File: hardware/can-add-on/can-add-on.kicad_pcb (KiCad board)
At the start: 2 copper layers, 48 x 40 mm, 38 parts

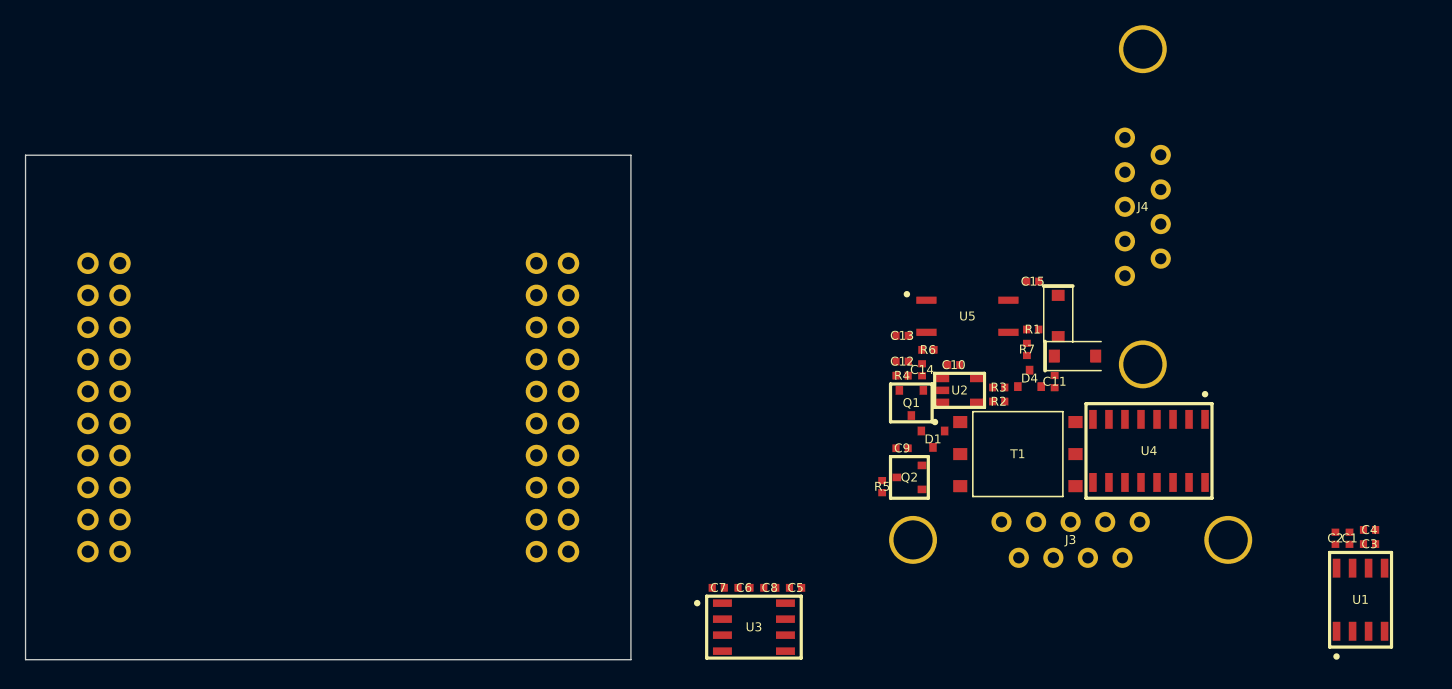
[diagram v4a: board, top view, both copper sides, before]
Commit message: Regenerate kicad with power/gnd symbols
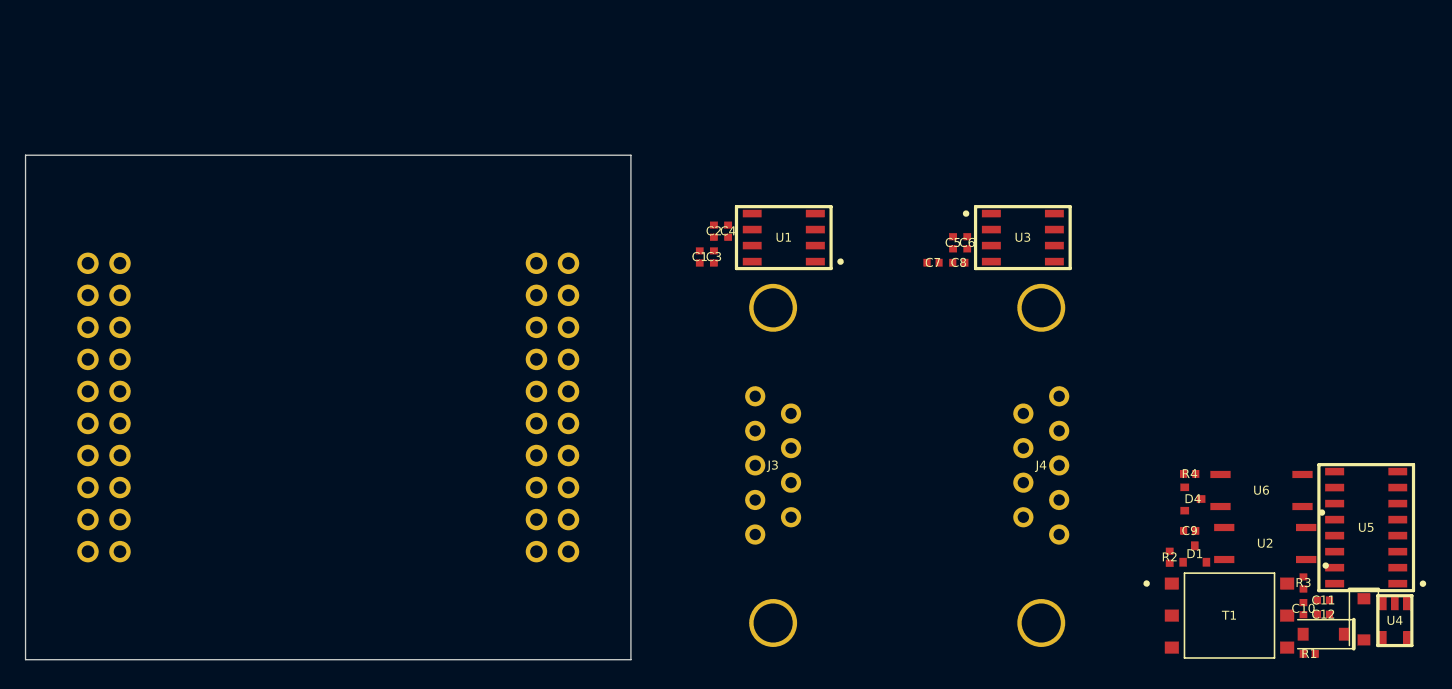
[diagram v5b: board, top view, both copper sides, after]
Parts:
- removed the ? at (206.4, 97.7)
- removed the ? at (207.7, 100.9)
- removed C13, C14, C15, R5, R6, R7: , can-add-on:ipc-two-pin-package$30
- removed Q1, Q2: , can-add-on:SOT95P280X100-3N
- added ?: , can-add-on:two-pin-polarized-package$58, F.Cu at (230.6, 121.8)
- added ?: , can-add-on:two-pin-polarized-package$58, F.Cu at (227.4, 123.0)
- added U6: , can-add-on:tlp-175, F.Cu at (222.5, 111.6)
- C1, C10, C11, C12, C2, C3, C4, C5, C6, C7, C8, C9, R1, R2, R3, R4: footprint can-add-on:ipc-two-pin-package$30 -> can-add-on:ipc-two-pin-package$28
- J1, J2: footprint can-add-on:pin-header-pkg$19 -> can-add-on:pin-header-pkg$17
- J3: footprint can-add-on:amphenol-delta-d-pkg$38 -> can-add-on:amphenol-delta-d-pkg$36
- J4: footprint can-add-on:amphenol-delta-d-pkg$38 -> can-add-on:amphenol-delta-d-pkg$50
- U1, U3: footprint can-add-on:soic127p-package$25 -> can-add-on:soic127p-package$23
- U2: footprint can-add-on:SOT95P280X145-5N -> can-add-on:tlp-175
- U4: footprint can-add-on:soic127p-package$75 -> can-add-on:SOT95P280X145-5N
- U5: footprint can-add-on:tlp-175 -> can-add-on:soic127p-package$65
- moved C3 56.7 mm to (179.1, 93.1), turned to 270 degrees
- moved C1 56.1 mm to (178.0, 93.1)
- moved C4 56.1 mm to (180.2, 91.0), turned to 270 degrees
- moved C2 55.0 mm to (179.1, 91.0), turned to 270 degrees
- moved U1 54.0 mm to (184.6, 91.5), turned to 180 degrees
- moved C12 39.0 mm to (227.4, 121.4), turned to 180 degrees
- moved U3 37.5 mm to (203.6, 91.5)
- moved U5 35.8 mm to (230.8, 114.5), turned to 180 degrees
- moved C10 33.8 mm to (225.8, 121.0), turned to 270 degrees
- moved R1 33.8 mm to (226.3, 124.5)
- moved C6 32.6 mm to (199.2, 91.9), turned to 90 degrees
- moved C7 30.9 mm to (196.5, 93.5)
- moved C5 30.1 mm to (198.0, 91.9), turned to 90 degrees
- moved C8 29.8 mm to (198.5, 93.5)
- moved R3 28.7 mm to (225.8, 118.9), turned to 90 degrees
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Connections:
- C10 pad 1: CANA-H -> VIO-B-ISO
- C10 pad 2: gnd -> ISO-GND
- C11 pad 1: VIO-B-ISO -> VIO-B
- C11 pad 2: net_xr-b_gnd -> gnd
- C12 pad 1: net_q$44_0_d -> VIO-B-ISO
- C12 pad 2: gnd -> ISO-GND
- C5 pad 2: net_xr-b_gnd -> ISO-GND
- C6 pad 2: net_xr-b_gnd -> ISO-GND
- C7 pad 2: net_xr-b_gnd -> ISO-GND
- C8 pad 2: net_xr-b_gnd -> ISO-GND
- C9 pad 1: CANA-L -> VIO-B
- D4 pad 1: net_j-b_p3 -> net_rid$71_p1
- D4 pad 2: net_ssr$79_drain1 -> net_j-b_p5
- D4 pad 3: net_xr-b_gnd -> ISO-GND
- J1 pad 1: net_iso$71_en1 -> VIO-B
- J4 pad 10: net_xr-b_gnd -> ISO-GND
- J4 pad 11: net_xr-b_gnd -> ISO-GND
- J4 pad 2: net_xr-b_gnd -> ISO-GND
- J4 pad 3: net_j-b_p3 -> net_rid$71_p1
- J4 pad 5: net_ssr$79_drain1 -> net_j-b_p5
- R1 pad 1: CANA-H -> glasgow_PA4
- R1 pad 2: net_q$44_0_s -> net_ssr$42_a
- R2 pad 1: CANA-L -> CANA-H
- R2 pad 2: net_rid$49_p2 -> net_rid$47_p2
- R3 pad 1: glasgow_PA4 -> glasgow_PB4
- R3 pad 2: net_q$44_0_g -> net_ssr$69_a
- R4 pad 1: net_q$44_0_g -> net_rid$71_p1
- R4 pad 2: gnd -> net_rid$71_p2
- T1 pad 1: net_iso$61_xfrmr_p1 -> net_iso$51_xfrmr_p1
- T1 pad 2: net_iso$71_en1 -> VIO-B
- T1 pad 3: net_iso$61_xfrmr_p3 -> net_iso$51_xfrmr_p3
- T1 pad 4: net_iso$61_xfrmr_p4 -> net_iso$51_xfrmr_p4
- T1 pad 5: net_xr-b_gnd -> ISO-GND
- T1 pad 6: net_iso$61_xfrmr_p6 -> net_iso$51_xfrmr_p6
- U2 pad 1: net_iso$61_xfrmr_p3 -> net_ssr$42_a
- U2 pad 3: net_iso$61_xfrmr_p1 -> gnd
- U2 pad 4: gnd -> net_rid$47_p2
- U3 pad 2: net_xr-b_gnd -> ISO-GND
- U3 pad 6: net_ssr$79_drain1 -> net_j-b_p5
- U3 pad 7: net_j-b_p3 -> net_rid$71_p1
- U4 pad 1: net_iso$71_en1 -> net_iso$51_xfrmr_p3
- U4 pad 2: gnd -> VIO-B
- U4 pad 3: glasgow_PB1 -> net_iso$51_xfrmr_p1
- U4 pad 4: glasgow_PB3 -> gnd
- U4 pad 5: net_iso$71_vdd1-in2 -> gnd
- U5 pad 1: net_ssr$79_a -> VIO-B
- U5 pad 3: gnd -> glasgow_PB1
- U5 pad 4: net_ssr$79_drain2 -> glasgow_PB3
- U5 pad 6: net_ssr$79_drain1 -> glasgow_PB2
